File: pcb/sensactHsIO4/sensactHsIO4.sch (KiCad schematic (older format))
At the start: 39 parts, among them J1 Bus, J2 PROG, J3 OUT0-3, J4 IN0-3 IO4-7, J5 IO8-15, J6 PSU+BUS, J7 L- L+ R- R+, SW1 BOOT, SW2 TERM OFF ON, U1 ESP32-WROOM-32U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

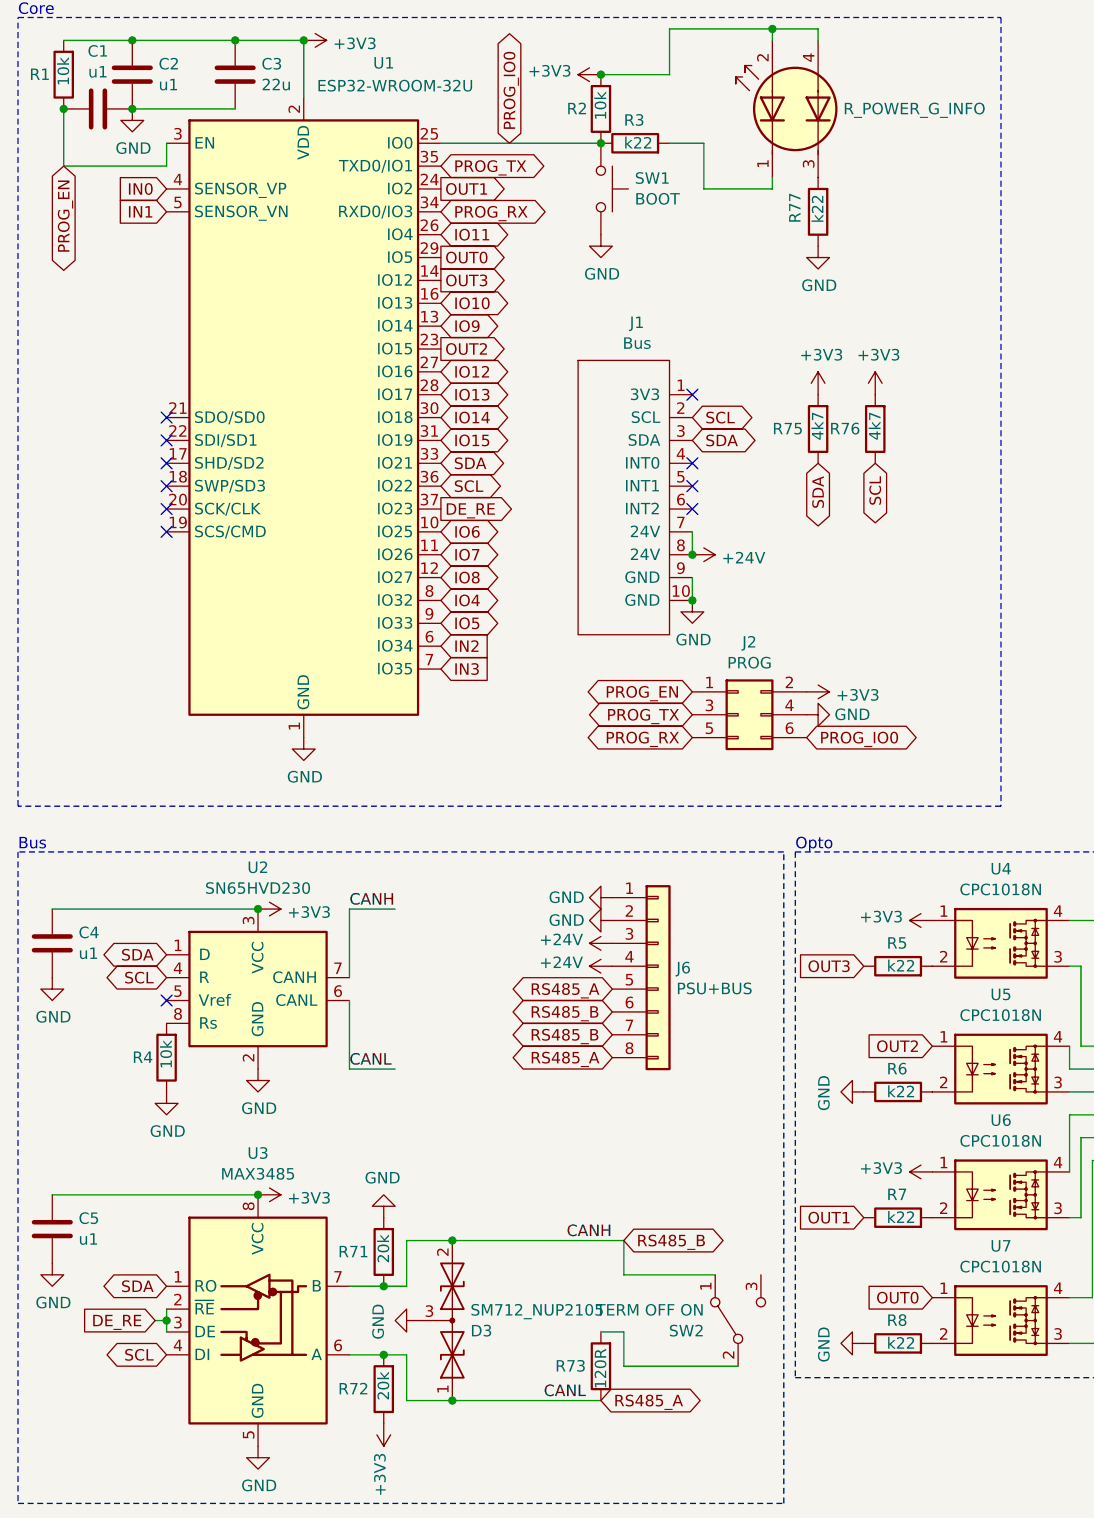
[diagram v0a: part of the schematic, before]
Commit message: Improvements in pcb design of sensactOutdoor and sensactHsIO4
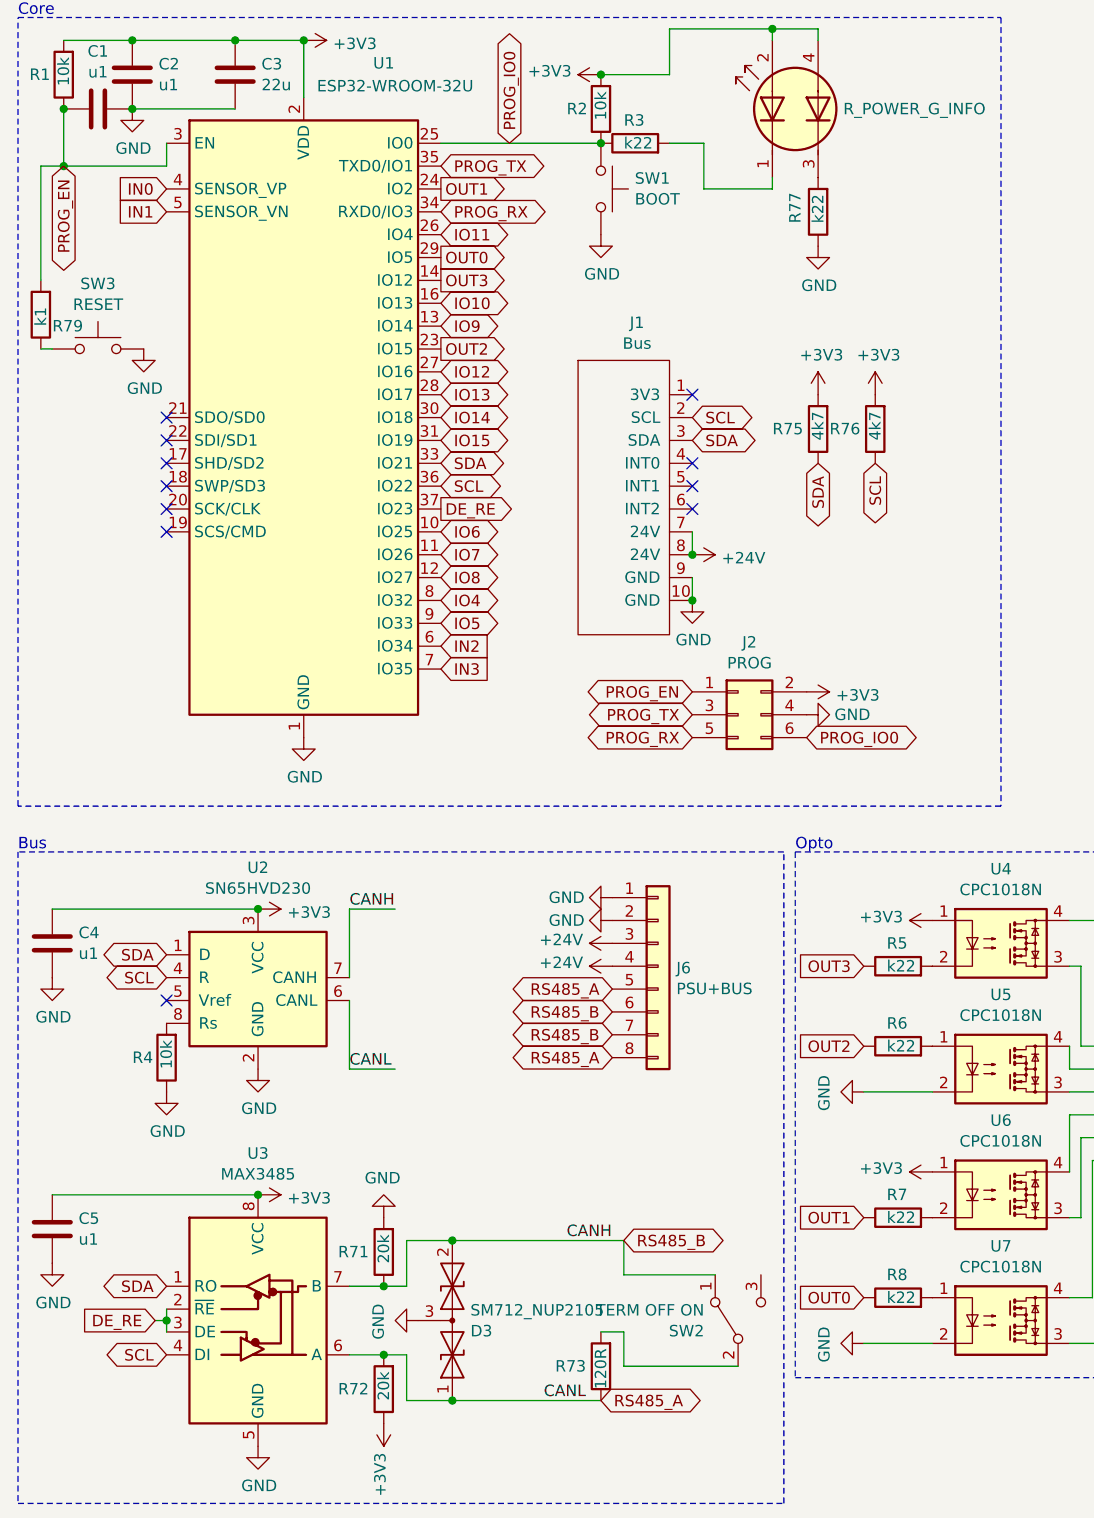
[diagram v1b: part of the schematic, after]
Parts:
- added R79: k1, Resistor_SMD:R_0805_2012Metric_Pad1.20x1.40mm_HandSolder, symbol Device:R
- added SW3: RESET, sensact:SW_SPST_2x4x3,5, symbol Switch:SW_Push
- J2: footprint Connector_IDC:IDC-Header_2x03_P2.54mm_Vertical -> liebler_CONN:IDC_2x03_P1.27mm_Vertical
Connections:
- net GND: now also U5.2, U7.2, SW3.2; no longer R6.1, R8.1
- net OUT0: now also R8.1; no longer U7.1
- net OUT2: now also R6.1; no longer U5.1
- net PROG_EN: now also R79.2
- net at R6.2: now also U5.1; no longer U5.2
- net at R8.2: now also U7.1; no longer U7.2
- new net: R79.1, SW3.1
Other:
- moved on the sheet: R6, R8
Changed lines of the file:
@@
 L Device:R R6
 U 1 1 6059FB55
-P 4400 5400
-F 0 "R6" V 4500 5450 50  0000 R CNN
-F 1 "k22" V 4400 5450 50  0000 R CNN
-F 2 "Resistor_SMD:R_0805_2012Metric_Pad1.20x1.40mm_HandSolder" V 4330 5400 50  0001 C CNN
-F 3 "~" H 4400 5400 50  0001 C CNN
-	1    4400 5400
-	0    -1   -1   0
-$EndComp
-Text GLabel 4550 6300 0    50   Input ~ 0
+P 4400 5200
+F 0 "R6" V 4500 5250 50  0000 R CNN
+F 1 "k22" V 4400 5250 50  0000 R CNN
+F 2 "Resistor_SMD:R_0805_2012Metric_Pad1.20x1.40mm_HandSolder" V 4330 5200 50  0001 C CNN
+F 3 "~" H 4400 5200 50  0001 C CNN
+	1    4400 5200
+	0    -1   -1   0
+$EndComp
+Text GLabel 4250 6300 0    50   Input ~ 0
 OUT0
 Text GLabel 4250 5950 0    50   Input ~ 0
 OUT1
-Text GLabel 4550 5200 0    50   Input ~ 0
+Text GLabel 4250 5200 0    50   Input ~ 0
 OUT2
 Text GLabel 4250 4850 0    50   Input ~ 0
@@
 L Device:R R8
 U 1 1 605A5993
-P 4400 6500
-F 0 "R8" V 4500 6550 50  0000 R CNN
-F 1 "k22" V 4400 6550 50  0000 R CNN
-F 2 "Resistor_SMD:R_0805_2012Metric_Pad1.20x1.40mm_HandSolder" V 4330 6500 50  0001 C CNN
-F 3 "~" H 4400 6500 50  0001 C CNN
-	1    4400 6500
+P 4400 6300
+F 0 "R8" V 4500 6350 50  0000 R CNN
+F 1 "k22" V 4400 6350 50  0000 R CNN
+F 2 "Resistor_SMD:R_0805_2012Metric_Pad1.20x1.40mm_HandSolder" V 4330 6300 50  0001 C CNN
+F 3 "~" H 4400 6300 50  0001 C CNN
+	1    4400 6300
 	0    -1   -1   0
 $EndComp
@@
 F 0 "J2" H 3750 4067 50  0000 C CNN
 F 1 "PROG" H 3750 3976 50  0000 C CNN
-F 2 "Connector_IDC:IDC-Header_2x03_P2.54mm_Vertical" H 3700 3750 50  0001 C CNN
+F 2 "liebler_CONN:IDC_2x03_P1.27mm_Vertical" H 3700 3750 50  0001 C CNN
 F 3 "~" H 3700 3750 50  0001 C CNN
 	1    3700 3750
@@
 F8 "AUDIO_R_P" O R 7950 1550 50
 $EndSheet
+Wire Wire Line
+	4550 5400 4250 5400
+Wire Wire Line
+	4550 6500 4250 6500
+$Comp
+L Switch:SW_Push SW3
+U 1 1 607D99BB
+P 900 2150
+F 0 "SW3" H 900 2435 50  0000 C CNN
+F 1 "RESET" H 900 2344 50  0000 C CNN
+F 2 "sensact:SW_SPST_2x4x3,5" H 900 2350 50  0001 C CNN
+F 3 "~" H 900 2350 50  0001 C CNN
+	1    900  2150
+	1    0    0    -1
+$EndComp
+Wire Wire Line
+	750  1350 650  1350
+Wire Wire Line
+	650  1350 650  1850
+Wire Wire Line
+	650  2150 700  2150
+Connection ~ 750  1350
+$Comp
+L Device:R R79
+U 1 1 607DCF60
+P 650 2000
+F 0 "R79" H 600 2050 50  0000 R CNN
+F 1 "k1" V 650 2050 50  0000 R CNN
+F 2 "Resistor_SMD:R_0805_2012Metric_Pad1.20x1.40mm_HandSolder" V 580 2000 50  0001 C CNN
+F 3 "~" H 650 2000 50  0001 C CNN
+	1    650  2000
+	-1   0    0    1
+$EndComp
+$Comp
+L power:GND #PWR079
+U 1 1 607DD6AE
+P 1100 2150
+F 0 "#PWR079" H 1100 1900 50  0001 C CNN
+F 1 "GND" H 1105 1977 50  0000 C CNN
+F 2 "" H 1100 2150 50  0001 C CNN
+F 3 "" H 1100 2150 50  0001 C CNN
+	1    1100 2150
+	1    0    0    -1
+$EndComp
 $EndSCHEMATC

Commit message: various changes
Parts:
- removed J6: PSU+BUS, liebler_CONN:PhoenixContact_MC_0,5_8-G-2.5_1x08_P2.50mm_Horizontal, symbol Connector_Generic:Conn_01x08
- removed U2: SN65HVD230, sensact:SOIC-8_3.9x4.9mm_Pitch1.27mm_handsolder, symbol Interface_CAN_LIN:SN65HVD230
- removed U3: MAX3485, sensact:SOIC-8_3.9x4.9mm_Pitch1.27mm_handsolder, symbol Interface_UART:MAX3485
- added C30: 1u, Capacitor_SMD:C_1206_3216Metric_Pad1.33x1.80mm_HandSolder, symbol Device:C
- added C31: 1u, Capacitor_SMD:C_0805_2012Metric_Pad1.18x1.45mm_HandSolder, symbol Device:C
- added J11: BUS, Connector_Phoenix_MC:PhoenixContact_MC_1,5_4-G-3.5_1x04_P3.50mm_Horizontal, symbol Connector_Generic:Conn_01x04
- added J12: 24V, Connector_Phoenix_MC:PhoenixContact_MC_1,5_2-G-3.5_1x02_P3.50mm_Horizontal, symbol Connector_Generic:Conn_01x02
- added J6: AIN, Connector_JST:JST_XH_B4B-XH-AM_1x04_P2.50mm_Vertical, symbol Connector_Generic:Conn_01x04
- added R80, R81, R82, R83, R84: 4k7, Resistor_SMD:R_0805_2012Metric_Pad1.20x1.40mm_HandSolder, symbol Device:R
- added R85, R86, R87, R88: 2k2, Resistor_SMD:R_0805_2012Metric_Pad1.20x1.40mm_HandSolder, symbol Device:R
- added SW4: INT0, liebler_MECH:SS12D00, symbol Switch:SW_SPDT
- added SW5: INT1, liebler_MECH:SS12D00, symbol Switch:SW_SPDT
- added SW6: INT2, liebler_MECH:SS12D00, symbol Switch:SW_SPDT
- added U2: ISO1050DUB, liebler_SEMICONDUCTORS:SOP-8_6.62x9.15mm_P2.54mm_handsolder, symbol Interface_CAN_LIN:ISO1050DUB
- added U3: ADS1115IDGS, Package_SO:TSSOP-10_3x3mm_P0.5mm, symbol Analog_ADC:ADS1115IDGS
- C4: value u1 -> 10u; footprint Capacitor_SMD:C_0805_2012Metric_Pad1.18x1.45mm_HandSolder -> Capacitor_SMD:C_1206_3216Metric_Pad1.33x1.80mm_HandSolder
- D3: value SM712_NUP2105 -> NUP2105
- R4: value 10k -> isI2C; footprint Resistor_SMD:R_0805_2012Metric_Pad1.20x1.40mm_HandSolder -> Resistor_SMD:R_1206_3216Metric_Pad1.30x1.75mm_HandSolder
- R71: value 20k -> isI2C; footprint Resistor_SMD:R_0805_2012Metric_Pad1.20x1.40mm_HandSolder -> Resistor_SMD:R_1206_3216Metric_Pad1.30x1.75mm_HandSolder
- R72: value 20k -> 4k7
- R75, R76: footprint Resistor_SMD:R_0805_2012Metric_Pad1.20x1.40mm_HandSolder -> Resistor_SMD:R_1206_3216Metric_Pad1.30x1.75mm_HandSolder
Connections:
- net +24V: now also C30.1, J12.2 (Pin_2)
- net +3V3: now also R72.2, C31.1, R80.2, U2.1 (VCC1), U3.8 (VDD); no longer C4.1, R72.1
- net GND: now also C30.2, C31.2, J12.1 (Pin_1), R85.2, R86.2, R87.2, R88.2, U2.4 (GND1), U3.1 (ADDR), U3.3 (GND); no longer C4.2, D3.3 (common), R4.1, R71.2
- net IO14: now also R80.1, U3.9 (SDA)
- net IO15: now also R72.1, U3.10 (SCL)
- net +5VA: now reaches J1.4 (INT0)
- net +5VA: now also C4.1, SW4.2 (B), SW4.3 (C), U2.8 (VCC2)
- net at J1.5 (INT1): now also SW5.2 (B), SW5.3 (C)
- net GNDA: now reaches J1.6 (INT2)
- net GNDA: now also C4.2, D3.3 (common), SW6.2 (B), SW6.3 (C), U2.5 (GND2)
- net CANR: now reaches R4.2
- net CANR: now also U1.36 (IO22), U2.2 (RXD)
- net DE_RE renamed IRQ
- net IRQ: now also SW4.1 (A), SW5.1 (A), SW6.1 (A)
- removed net RS485_A: D3.1 (A1), R72.2, R73.1
- net RS485_B renamed CANL
- net CANL: now also D3.1 (A1), J1.3 (SDA), R76.1, J11.2 (Pin_2), J11.3 (Pin_3), U2.6 (CANL); no longer D3.2 (A2)
- removed net SCL: J1.2 (SCL), R76.1, U1.36 (IO22)
- removed net SDA: J1.3 (SDA), R75.1, U1.33 (IO21)
- new net: R83.2, R87.1, U3.4 (AIN0)
- new net: R84.2, R88.1, U3.5 (AIN1)
- new net: R81.2, R85.1, U3.6 (AIN2)
- new net: R82.2, R86.1, U3.7 (AIN3)
- new net: J6.1 (Pin_1), R81.1
- new net: J6.2 (Pin_2), R82.1
- new net: J6.3 (Pin_3), R83.1
- new net: J6.4 (Pin_4), R84.1
- new net CANH: D3.2 (A2), J1.2 (SCL), J11.1 (Pin_1), J11.4 (Pin_4), R4.1, R73.1, R75.1, U2.7 (CANH)
- new net CANT: R71.2, U1.33 (IO21), U2.3 (TXD)
- no-connect marks 11 -> 8
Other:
- moved on the sheet: C5, D3, J2, J3, R5, R6, R7, R73, R75, R76, R8, SW2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

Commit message: Renamed liebler_IC to liebler_SEMICONDUCTORS
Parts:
- U4, U5, U6, U7: footprint liebler_IC:SOP-4_3.8x4.1mm_P2.54mm_handsolder -> liebler_SEMICONDUCTORS:SOP-4_3.8x4.1mm_P2.54mm_handsolder
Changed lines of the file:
@@
 F 0 "U4" H 9500 4575 50  0000 C CNN
 F 1 "CPC1018N" H 9500 4484 50  0000 C CNN
-F 2 "liebler_IC:SOP-4_3.8x4.1mm_P2.54mm_handsolder" H 9300 4050 50  0001 L CIN
+F 2 "liebler_SEMICONDUCTORS:SOP-4_3.8x4.1mm_P2.54mm_handsolder" H 9300 4050 50  0001 L CIN
 F 3 "http://www.ixysic.com/home/pdfs.nsf/www/CPC1017N.pdf/$file/CPC1017N.pdf" H 9450 4250 50  0001 L CNN
 	1    9500 4250
@@
 F 0 "U5" H 9500 5125 50  0000 C CNN
 F 1 "CPC1018N" H 9500 5034 50  0000 C CNN
-F 2 "liebler_IC:SOP-4_3.8x4.1mm_P2.54mm_handsolder" H 9300 4600 50  0001 L CIN
+F 2 "liebler_SEMICONDUCTORS:SOP-4_3.8x4.1mm_P2.54mm_handsolder" H 9300 4600 50  0001 L CIN
 F 3 "http://www.ixysic.com/home/pdfs.nsf/www/CPC1017N.pdf/$file/CPC1017N.pdf" H 9450 4800 50  0001 L CNN
 	1    9500 4800
@@
 F 0 "U6" H 9500 5675 50  0000 C CNN
 F 1 "CPC1018N" H 9500 5584 50  0000 C CNN
-F 2 "liebler_IC:SOP-4_3.8x4.1mm_P2.54mm_handsolder" H 9300 5150 50  0001 L CIN
+F 2 "liebler_SEMICONDUCTORS:SOP-4_3.8x4.1mm_P2.54mm_handsolder" H 9300 5150 50  0001 L CIN
 F 3 "http://www.ixysic.com/home/pdfs.nsf/www/CPC1017N.pdf/$file/CPC1017N.pdf" H 9450 5350 50  0001 L CNN
 	1    9500 5350
@@
 F 0 "U7" H 9500 6225 50  0000 C CNN
 F 1 "CPC1018N" H 9500 6134 50  0000 C CNN
-F 2 "liebler_IC:SOP-4_3.8x4.1mm_P2.54mm_handsolder" H 9300 5700 50  0001 L CIN
+F 2 "liebler_SEMICONDUCTORS:SOP-4_3.8x4.1mm_P2.54mm_handsolder" H 9300 5700 50  0001 L CIN
 F 3 "http://www.ixysic.com/home/pdfs.nsf/www/CPC1017N.pdf/$file/CPC1017N.pdf" H 9450 5900 50  0001 L CNN
 	1    9500 5900
